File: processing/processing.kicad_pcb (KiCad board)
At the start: 2 copper layers, 64 x 64 mm, 28 parts, among them J1 Conn_01x02, J2 Conn_01x03, J3 Conn_01x05, J4 HRO-TYPE-C-31-M-12, J5 ICSP, SW1 SW_RESET, U1 CH340G, U2 ATmega328P-AU, Y1 12MHz, Y2 16MHz

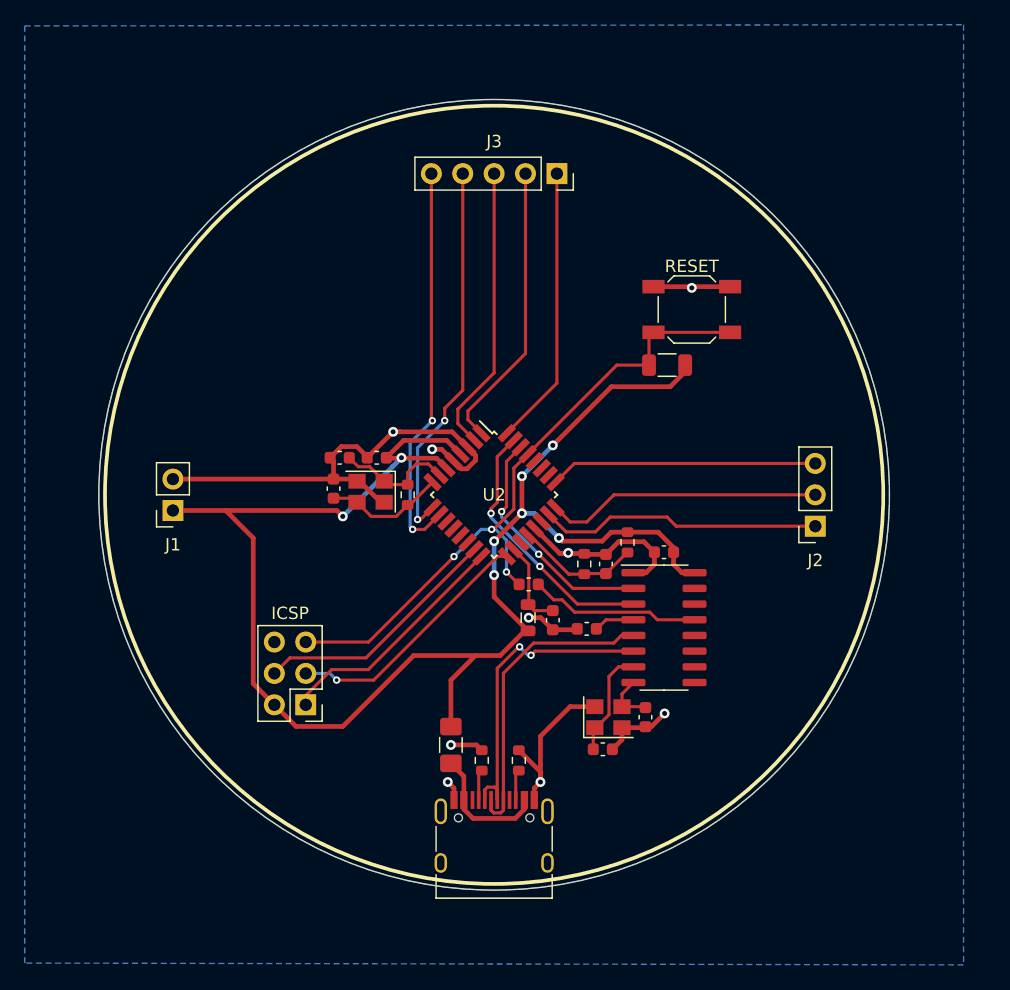
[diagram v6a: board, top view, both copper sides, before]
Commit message: errata 2: fix footprints
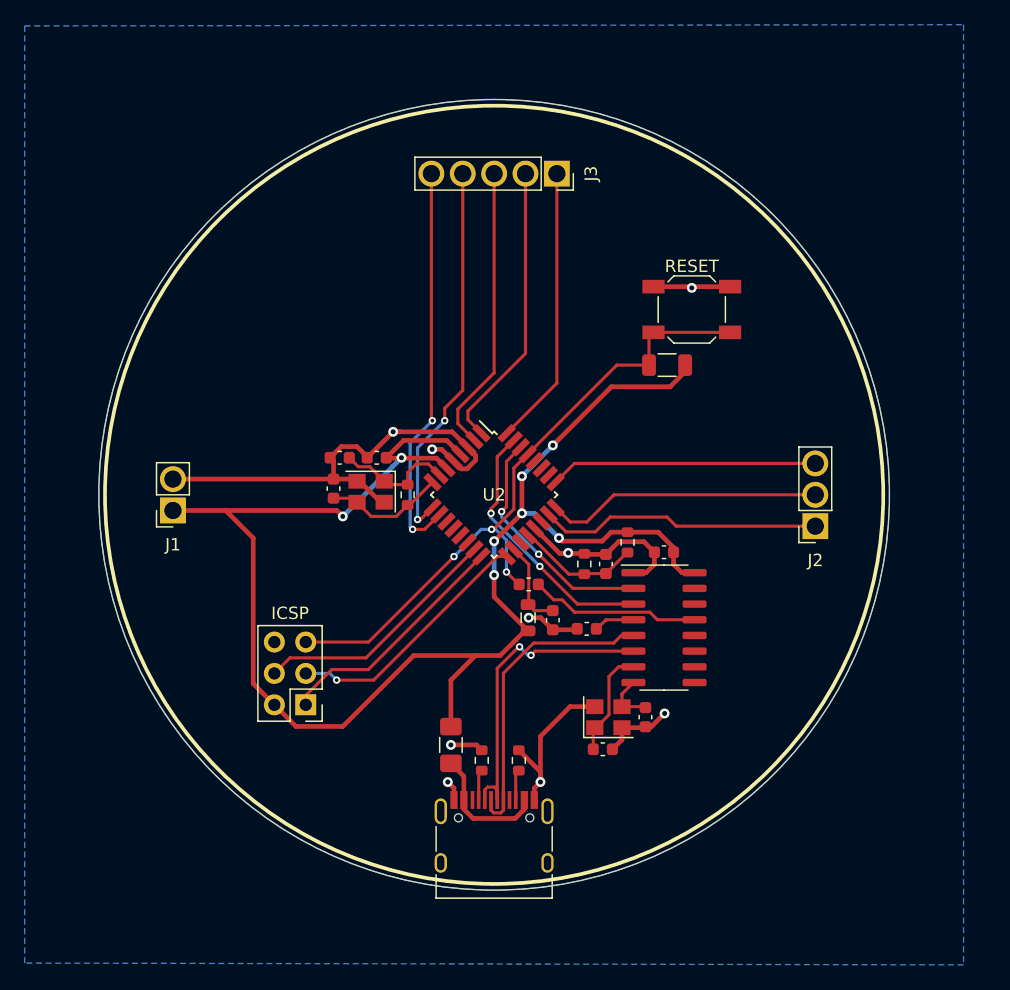
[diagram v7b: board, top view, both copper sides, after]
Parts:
- J1: footprint Connector_PinSocket_2.54mm:PinSocket_1x02_P2.54mm_Vertical -> df-parts:310-XX-102-41-001000
- J2: footprint Connector_PinSocket_2.54mm:PinSocket_1x03_P2.54mm_Vertical -> df-parts:310-XX-103-41-001000
- J3: footprint Connector_PinSocket_2.54mm:PinSocket_1x05_P2.54mm_Vertical -> df-parts:310-XX-105-41-001000
